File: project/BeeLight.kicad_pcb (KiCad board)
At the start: 2 copper layers, 32 x 24 mm, 25 parts, among them IC101 BT40F, IC102 APDS-9306-065, IC103 BME688, Q101 BSS84, SW101 JOIN, X102 DEBUG

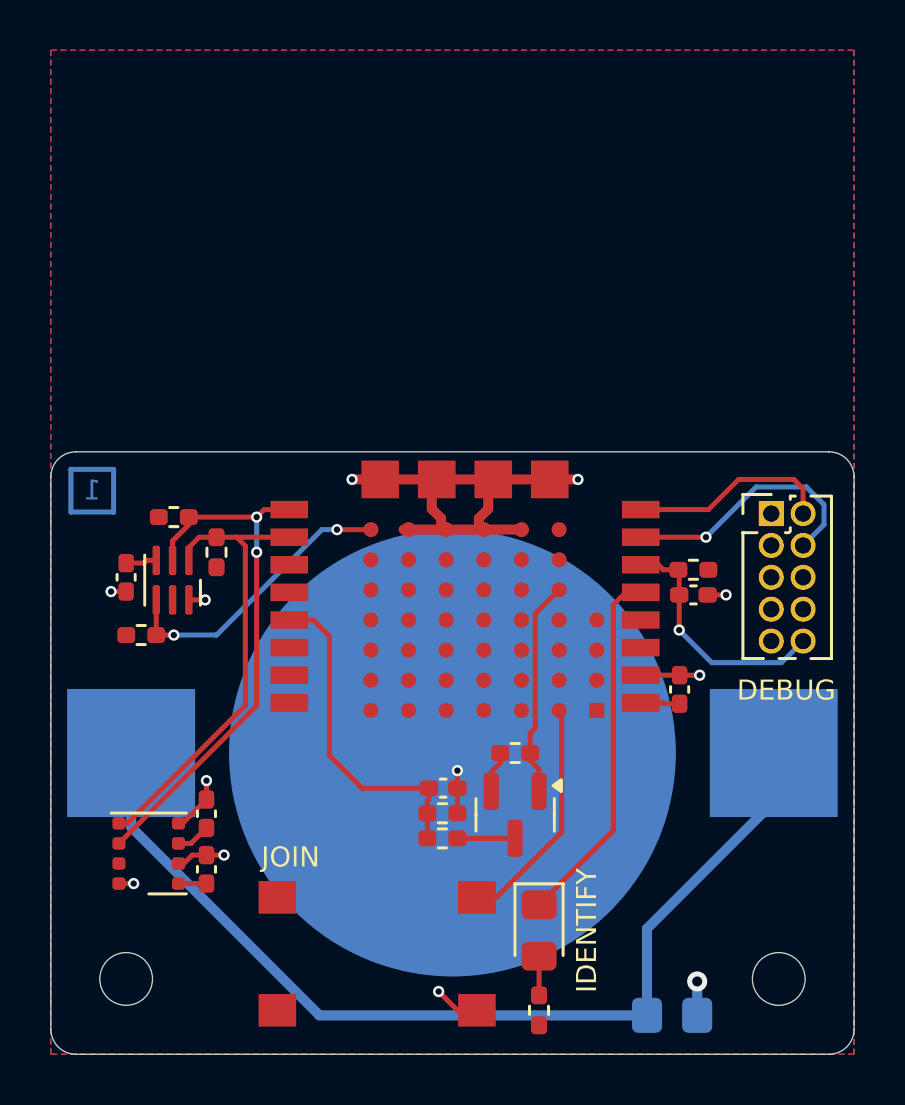
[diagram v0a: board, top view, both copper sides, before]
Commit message: Firmware is compiling with custom board, testing first hardware release
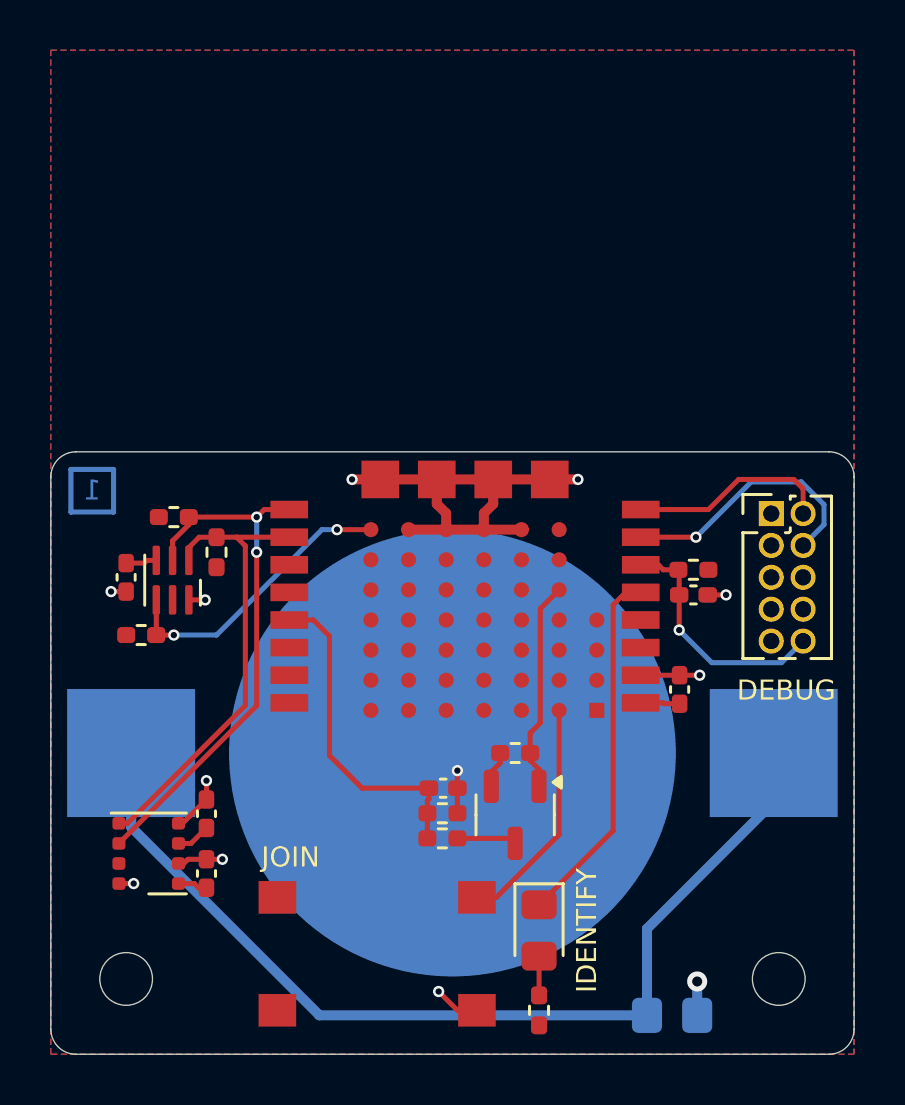
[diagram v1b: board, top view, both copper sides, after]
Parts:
- Q101: footprint Package_TO_SOT_SMD:SOT-23 -> Package_TO_SOT_SMD:SOT-23-3
- moved C105 0.17 mm to (128.2, 98.8)

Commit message: - Replace nRF53 with nRF54L - Working on version 2 with BME688
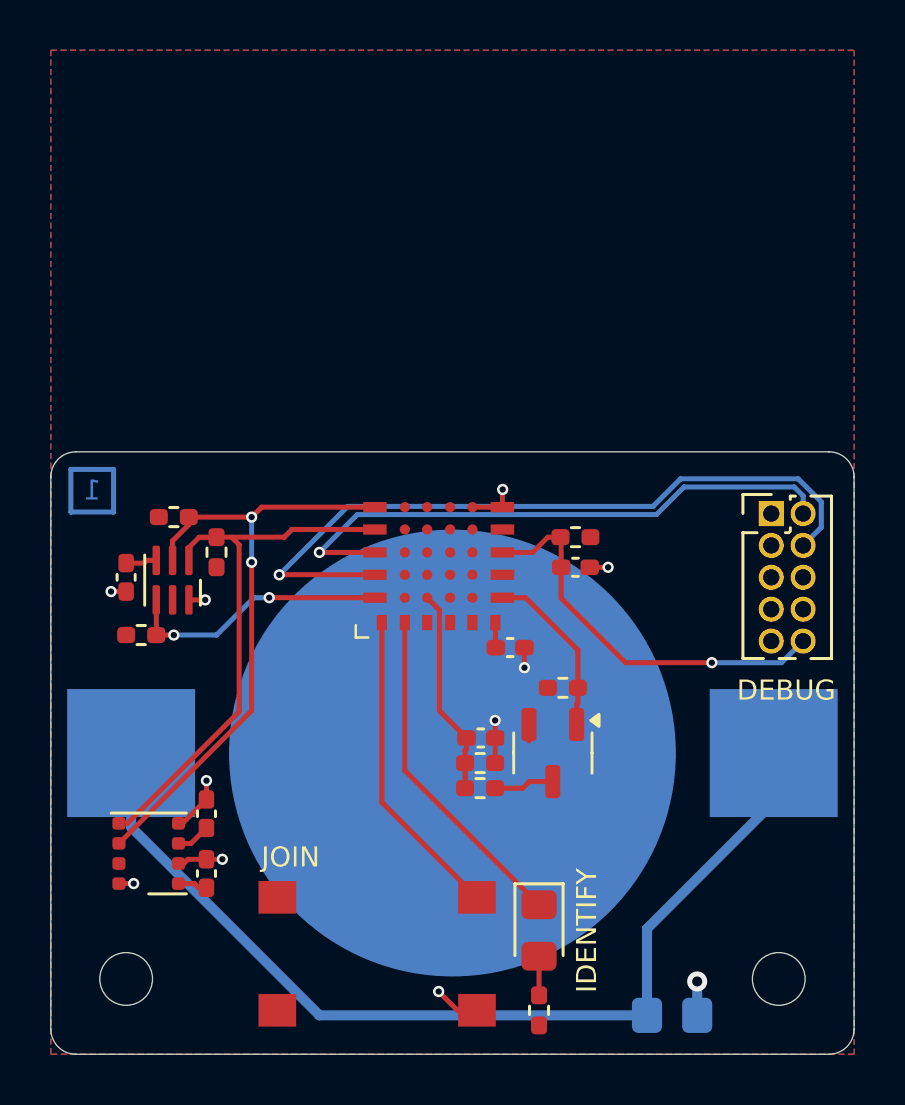
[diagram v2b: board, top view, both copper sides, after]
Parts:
- removed IC101: BT40F, Fanstel:XCVR_BT40F
- added M101: BC15C, Fanstel:BC15C, F.Cu at (138.0, 83.0)
- moved C102 6.95 mm to (140.3, 89.8), turned to 0 degrees
- moved R101 4.88 mm to (142.9, 85.4)
- moved C101 4.83 mm to (142.9, 86.6)
- moved R107 3.22 mm to (142.4, 91.4)
- moved Q101 2.88 mm to (142.0, 94.0)
- moved C103 2.50 mm to (139.1, 93.4)
- moved R108 2.50 mm to (139.1, 95.4)
- moved R109 2.50 mm to (139.1, 94.4)
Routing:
- net SWDCLK: track 10.6 -> 29.4 mm
- net GND: track 30.5 -> 12.9 mm, vias 11 -> 10
- net SWDIO: track 8.11 -> 23.4 mm, vias 0 -> 1
- net ~{RESET}: track 9.79 -> 16.1 mm
- net V_{BAT}: track 13.2 -> 8.27 mm
- net SCL: track 18.5 -> 21.9 mm
- net SDA: track 21.4 -> 24.8 mm
- net Net-(M101-P2.05): track 9.26 -> 12.5 mm
- net BAT_E: track 8.65 -> 6.86 mm
- net +BATT: track 8.38 -> 6.93 mm
- net INT: track 11.7 -> 10.7 mm
- net Net-(D101-K): track 14.3 -> 13.5 mm

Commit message: Switch to BM15C module
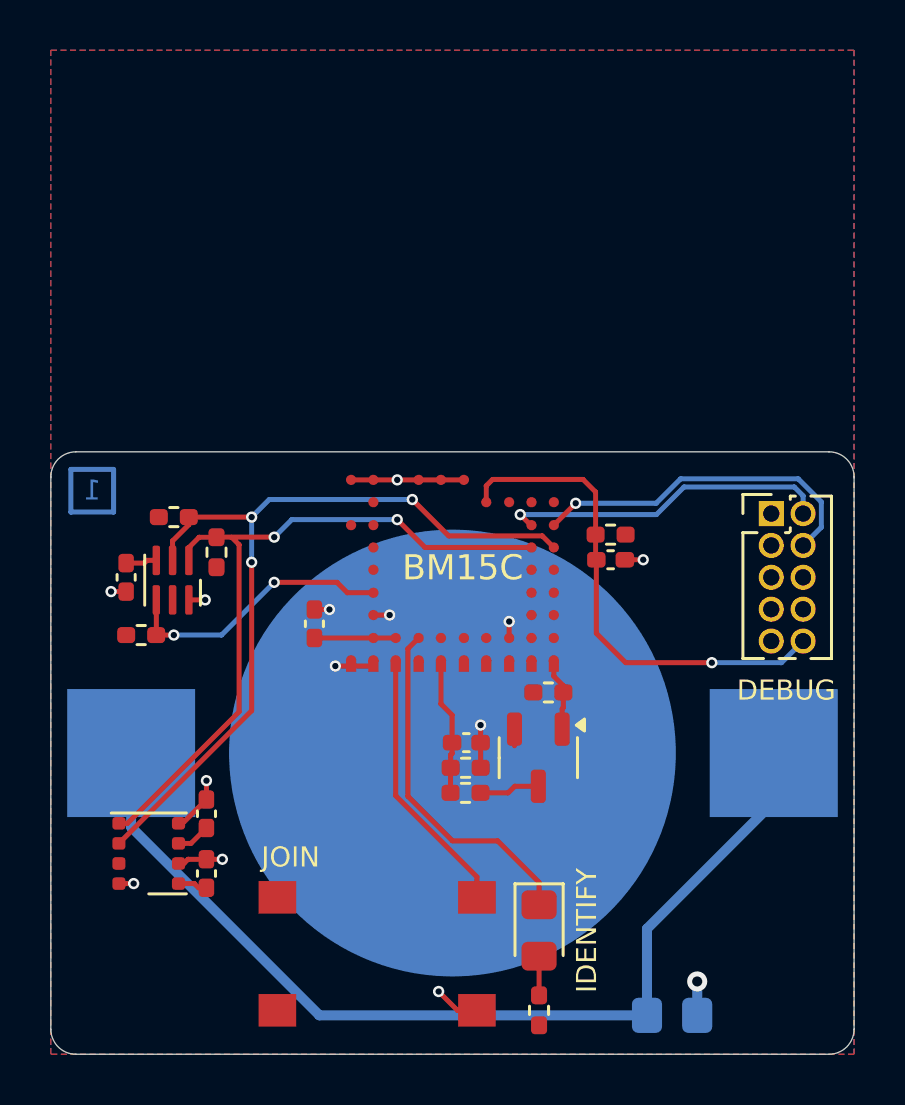
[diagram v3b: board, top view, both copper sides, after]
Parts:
- removed M101: BC15C, Fanstel:BC15C
- removed REF** (x2): MountingHole_2.1mm, MountingHole:MountingHole_2.1mm
- added M102: BC15C, Fanstel:BM15C, F.Cu at (138.0, 82.0)
- moved C102 7.86 mm to (132.5, 88.8), turned to 90 degrees
- moved C101 1.43 mm to (144.3, 86.3)
- moved R101 1.40 mm to (144.3, 85.3)
- moved Q101 0.61 mm to (141.4, 94.2)
- moved R107 0.61 mm to (141.8, 91.6)
- moved R108 0.61 mm to (138.5, 95.6)
- moved C103 0.61 mm to (138.6, 93.6)
- moved R109 0.61 mm to (138.5, 94.6)
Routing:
- net SWDCLK: track 29.4 -> 13.8 mm
- net SWDIO: track 23.4 -> 13.2 mm
- net SDA: track 24.8 -> 32.8 mm, vias 2 -> 3
- net SCL: track 21.9 -> 28.8 mm, vias 0 -> 2
- net GND: track 12.9 -> 18.1 mm, vias 10 -> 13
- net BAT_E: track 6.86 -> 2.69 mm
- net ~{RESET}: track 16.1 -> 20.0 mm
- net V_{BAT}: track 8.27 -> 5.27 mm
- net +BATT: track 6.93 -> 9.16 mm
- net Net-(M102-P1.01/32K): track 12.5 -> 10.6 mm
- net Net-(D101-K): track 13.5 -> 14.0 mm

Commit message: Replace nRF54 module
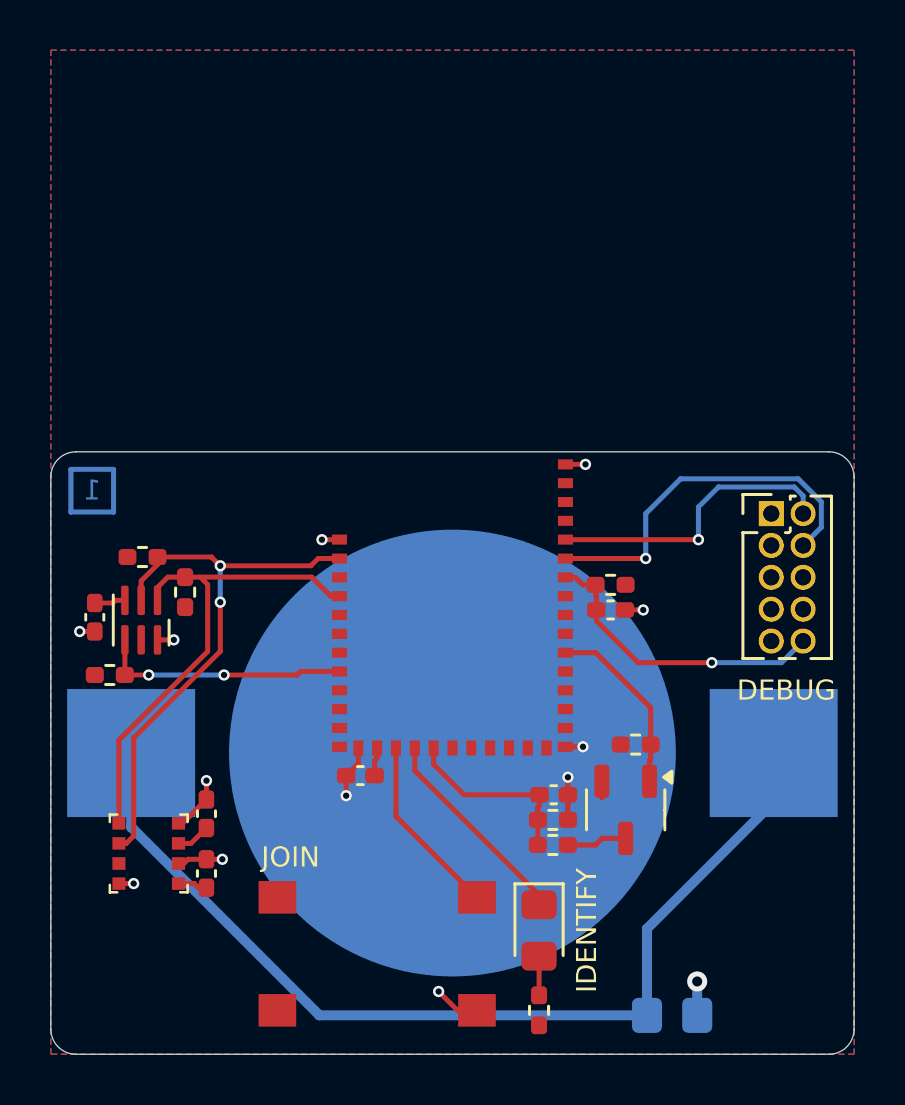
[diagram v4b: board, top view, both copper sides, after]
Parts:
- removed M102: BC15C, Fanstel:BM15C
- added M101: BL54L15, Ezurio:BL54L15, F.Cu at (138.0, 87.3)
- IC103: footprint Bosch:Bosch_LGA-8_3x3mm_P0.8mm_ClockwisePinNumbering -> Package_LGA_Kampi:Bosch_LGA-8_3x3mm_P0.8mm_ClockwisePinNumbering
- moved C102 6.32 mm to (134.3, 94.9), turned to 180 degrees
- moved Q101 4.05 mm to (144.9, 96.3)
- moved R107 4.05 mm to (145.3, 93.7)
- moved R108 4.05 mm to (142.0, 97.7)
- moved C103 4.05 mm to (142.0, 95.7)
- moved R109 4.05 mm to (142.0, 96.7)
- moved R104 2.02 mm to (125.7, 86.2)
- moved C104 2.02 mm to (123.8, 88.6)
- moved IC102 2.02 mm to (125.6, 88.7)
- moved R105 2.02 mm to (127.3, 87.6)
- moved R106 2.02 mm to (124.3, 90.9)
- moved C101 2.00 mm to (144.3, 88.3)
- moved R101 2.00 mm to (144.3, 87.3)
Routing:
- net SDA: track 32.8 -> 22.4 mm, vias 3 -> 2
- net SCL: track 28.8 -> 19.6 mm, vias 2 -> 0
- net ~{RESET}: track 20.0 -> 12.1 mm
- net Net-(D101-K): track 14.0 -> 8.30 mm
- net BAT_E: track 2.69 -> 7.25 mm
- net GND: track 18.1 -> 14.5 mm, vias 13 -> 12
- net Net-(M101-P1.00/32K): track 10.6 -> 7.29 mm
- net V_{BAT}: track 5.27 -> 7.40 mm
- net +BATT: track 9.16 -> 7.06 mm
- net SWDIO: track 13.2 -> 12.0 mm
- net SWDCLK: track 13.8 -> 15.0 mm
- net INT: track 11.1 -> 10.0 mm
